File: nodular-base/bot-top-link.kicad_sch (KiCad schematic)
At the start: 9 parts, among them J9 Conn_01x30_MountingPin, U13 MT9700, U6 74LVC1G17

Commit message: WIP layout for base
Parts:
- added C21, C22: 10uF, Capacitor_SMD:C_1206_3216Metric, symbol Device:C
- added D14: SK6805MICRO-J, LED_SMD:LED_SK6805_PLCC4_2.4x2.7mm_P1.3mm, symbol LED:SK6812MINI
- added R22 (x2): 11k3, Resistor_SMD:R_0402_1005Metric, symbol Device:R
- added R22 (x2): 1k, Resistor_SMD:R_0402_1005Metric, symbol Device:R
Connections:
- net GND: now also U13.2 (GND), U6.3 (GND), C21.2, C22.2, D14.2 (VSS), R22.2, R22.2
- net LED_DATA: now reaches U6.2
- net at U6.4: now also R22.1
- net TOP_VBAT_SW: now reaches U6.5 (VCC)
- net TOP_VBAT_SW: now also U13.1 (OUT), C22.1, D14.4 (VDD)
- net at U13.3 (SET): now also R22.1
- net LED_EN: now reaches U13.4 (ON)
- net LED_EN: now also R22.1
- net at U13.5 (IN): now also C21.1
- new net: D14.1 (DOUT), R22.1
- new net: D14.3 (DIN), R22.2
- new net LED_DATA_TOP: R22.2
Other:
- moved on the sheet: U6

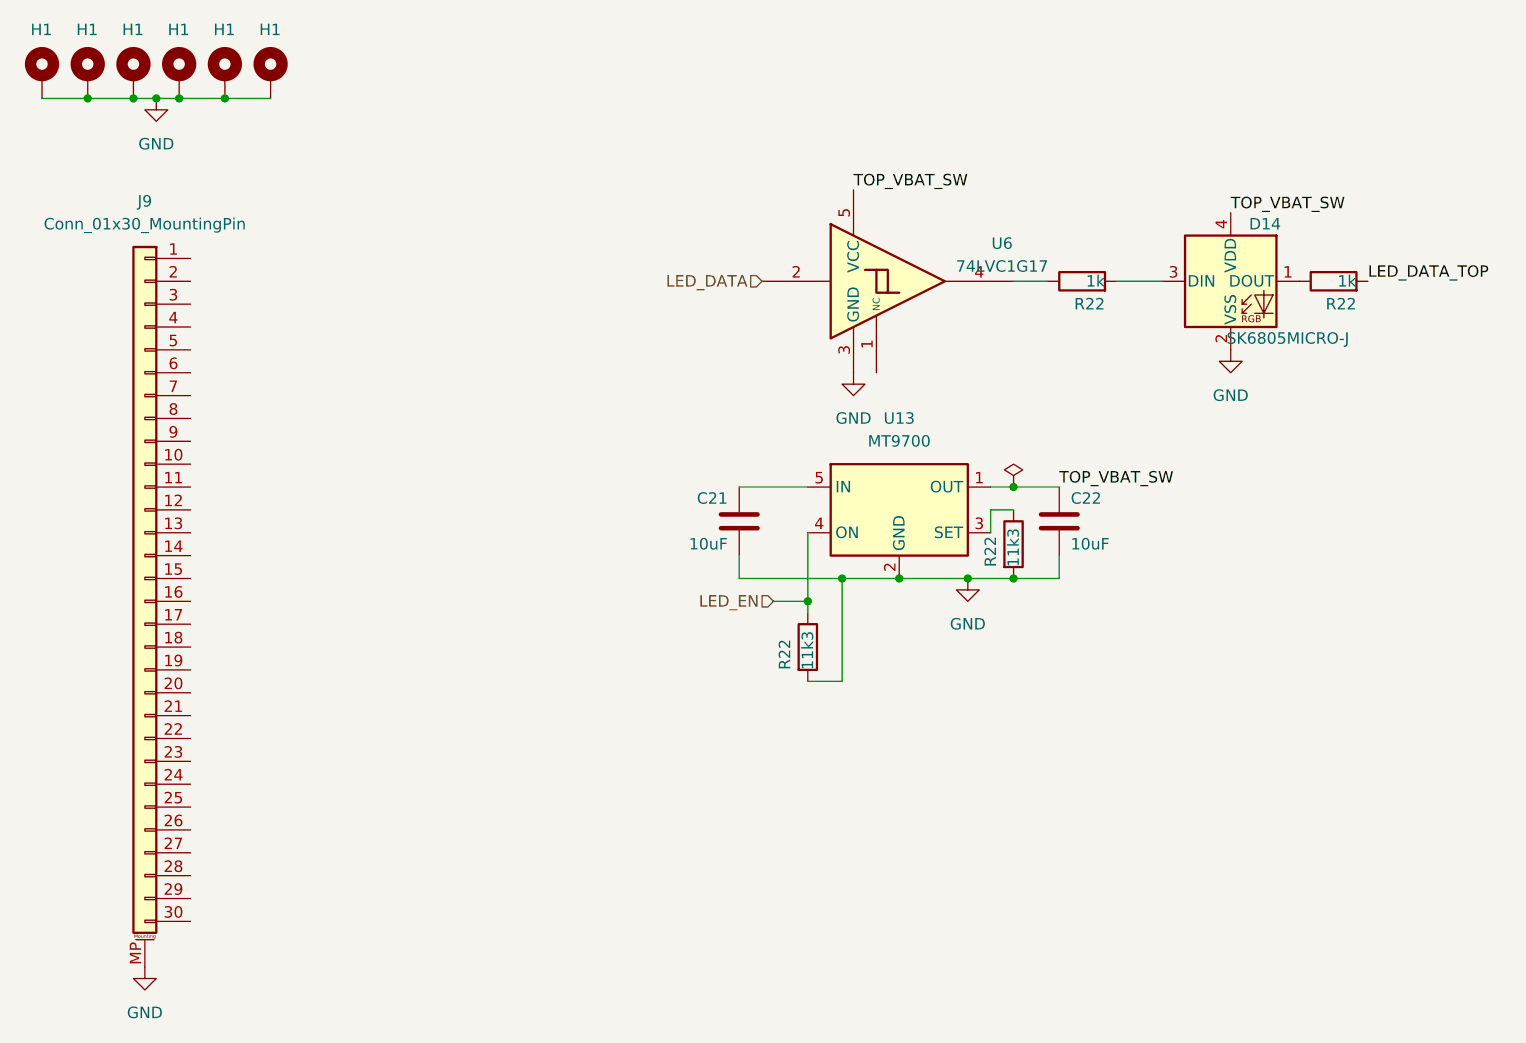
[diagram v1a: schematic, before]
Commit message: Switched from CAN to USB for second USB-C port Added second PD controller and USB mux to allow switching between host and device port Added SOICbite to corner All routing complete Updated pin map, added i2c addresses, soicbit pin mapping, and fpc pinout to document
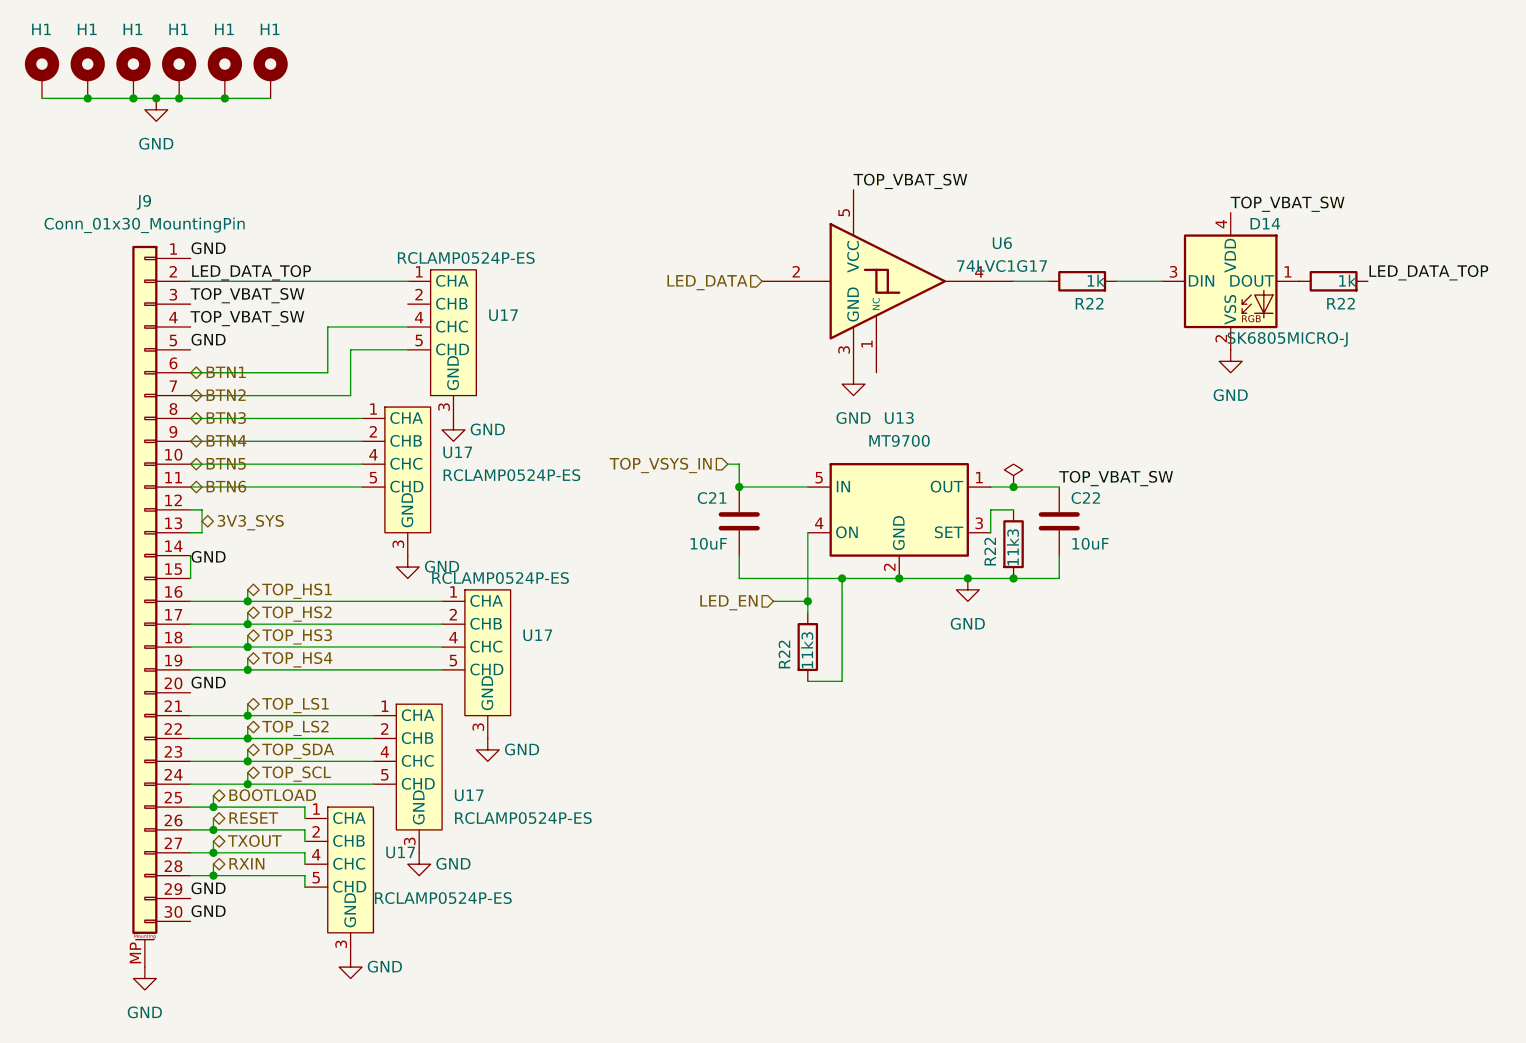
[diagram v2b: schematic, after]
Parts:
- added U17 (x5): RCLAMP0524P-ES, Package_DFN_QFN:Diodes_UDFN-10_1.0x2.5mm_P0.5mm, symbol nodular:RCLAMP0524P-ES
- J9: footprint Connector_FFC-FPC:Hirose_FH12-30S-0.5SH_1x30-1MP_P0.50mm_Horizontal -> nodular:Jushuo_AFC01-S30FCC-00_1x30-1MP_P0.50mm_Horizontal
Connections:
- net GND: now also J9.1 (Pin_1), J9.14 (Pin_14), J9.15 (Pin_15), J9.20 (Pin_20), J9.29 (Pin_29), J9.30 (Pin_30), J9.5 (Pin_5), U17.3 (GND), U17.3 (GND), U17.3 (GND), U17.3 (GND), U17.3 (GND), U17.8 (GND), U17.8 (GND), U17.8 (GND), U17.8 (GND), U17.8 (GND)
- net LED_DATA_TOP: now also J9.2 (Pin_2), U17.1 (CHA), U17.10 (CHA)
- net TOP_VBAT_SW: now also J9.3 (Pin_3), J9.4 (Pin_4)
- net TOP_VSYS_IN: now reaches C21.1, U13.5 (IN)
- net BTN5: now reaches J9.10 (Pin_10)
- net BTN5: now also U17.4 (CHC), U17.7 (CHC)
- net BTN6: now reaches J9.11 (Pin_11)
- net BTN6: now also U17.5 (CHD), U17.6 (CHD)
- net 3V3_SYS: now reaches J9.12 (Pin_12)
- net 3V3_SYS: now also J9.13 (Pin_13)
- net TOP_HS1: now reaches J9.16 (Pin_16)
- net TOP_HS1: now also U17.1 (CHA), U17.10 (CHA)
- net TOP_HS2: now reaches J9.17 (Pin_17)
- net TOP_HS2: now also U17.2 (CHB), U17.9 (CHB)
- net TOP_HS3: now reaches J9.18 (Pin_18)
- net TOP_HS3: now also U17.4 (CHC), U17.7 (CHC)
- net TOP_HS4: now reaches J9.19 (Pin_19)
- net TOP_HS4: now also U17.5 (CHD), U17.6 (CHD)
- net TOP_LS1: now reaches J9.21 (Pin_21)
- net TOP_LS1: now also U17.1 (CHA), U17.10 (CHA)
- net TOP_LS2: now reaches J9.22 (Pin_22)
- net TOP_LS2: now also U17.2 (CHB), U17.9 (CHB)
- net TOP_SDA: now reaches J9.23 (Pin_23)
- net TOP_SDA: now also U17.4 (CHC), U17.7 (CHC)
- net TOP_SCL: now reaches J9.24 (Pin_24)
- net TOP_SCL: now also U17.5 (CHD), U17.6 (CHD)
- net BOOTLOAD: now reaches J9.25 (Pin_25)
- net BOOTLOAD: now also U17.1 (CHA), U17.10 (CHA)
- net RESET: now reaches J9.26 (Pin_26)
- net RESET: now also U17.2 (CHB), U17.9 (CHB)
- net TXOUT: now reaches J9.27 (Pin_27)
- net TXOUT: now also U17.4 (CHC), U17.7 (CHC)
- net RXIN: now reaches J9.28 (Pin_28)
- net RXIN: now also U17.5 (CHD), U17.6 (CHD)
- net BTN1: now reaches J9.6 (Pin_6)
- net BTN1: now also U17.4 (CHC), U17.7 (CHC)
- net BTN2: now reaches J9.7 (Pin_7)
- net BTN2: now also U17.5 (CHD), U17.6 (CHD)
- net BTN3: now reaches J9.8 (Pin_8)
- net BTN3: now also U17.1 (CHA), U17.10 (CHA)
- net BTN4: now reaches J9.9 (Pin_9)
- net BTN4: now also U17.2 (CHB), U17.9 (CHB)
- new net: U17.2 (CHB), U17.9 (CHB)

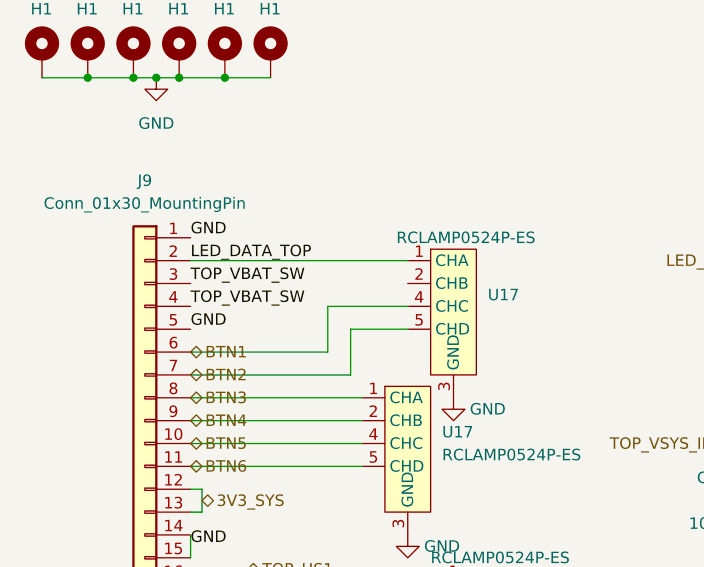
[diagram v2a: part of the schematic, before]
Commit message: Add VCONN support and load switch with 1.5A current limit on host port Add accelerometer interrupt connection Update BOM with important capacitor and inductor PNs and costings
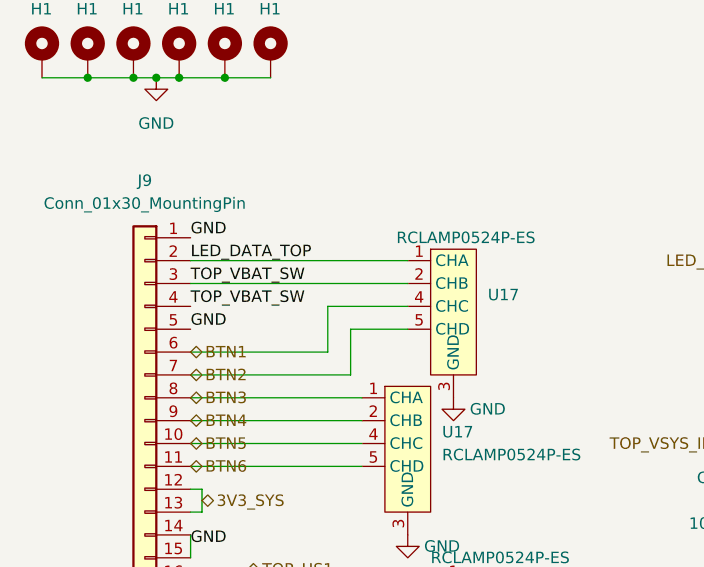
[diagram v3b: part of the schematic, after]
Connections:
- net TOP_VBAT_SW: now also U17.2 (CHB), U17.9 (CHB)
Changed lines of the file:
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@@
+    (stroke (width 0) (type default))
+  )
+  (wire (pts (xy 41.91 52.07) (xy 66.04 52.07))
     (stroke (width 0) (type default))
   )

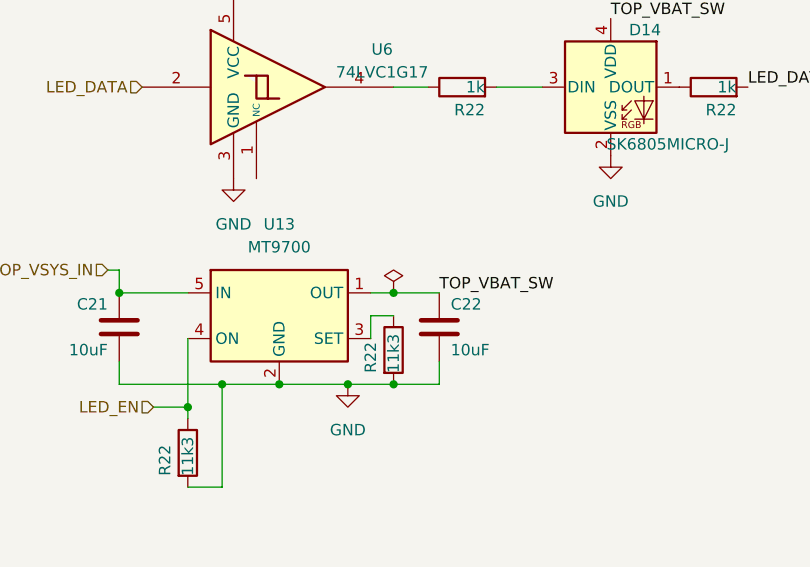
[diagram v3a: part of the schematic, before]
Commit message: Add 3d models and fix erc errors
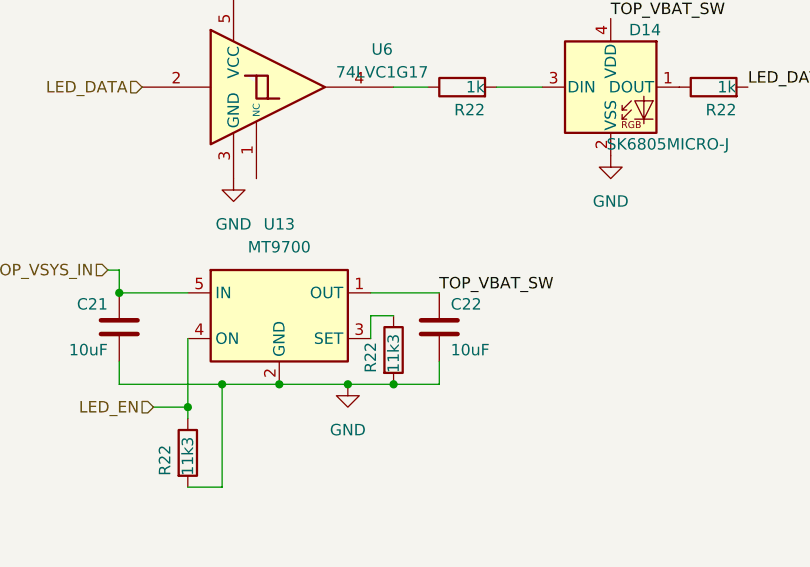
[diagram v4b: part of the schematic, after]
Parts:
- D14: footprint LED_SMD:LED_SK6805_PLCC4_2.4x2.7mm_P1.3mm -> nodular:LED_SK6805_PLCC4_2.4x2.7mm_P1.3mm
- U17: footprint Package_DFN_QFN:Diodes_UDFN-10_1.0x2.5mm_P0.5mm -> nodular:Diodes_UDFN-10_1.0x2.5mm_P0.5mm
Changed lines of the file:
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@@
   (junction (at 110.49 85.09) (diameter 0) (color 0 0 0 0)
   )
-  (junction (at 133.35 72.39) (diameter 0) (color 0 0 0 0)
-  )
   (junction (at 48.26 97.79) (diameter 0) (color 0 0 0 0)
   )
@@
     (stroke (width 0) (type default))
   )
-  (wire (pts (xy 130.81 72.39) (xy 133.35 72.39))
+  (wire (pts (xy 130.81 72.39) (xy 138.43 72.39))
     (stroke (width 0) (type default))
   )
@@
   )
   (wire (pts (xy 44.45 114.3) (xy 44.45 115.57))
-    (stroke (width 0) (type default))
-  )
-  (wire (pts (xy 133.35 72.39) (xy 138.43 72.39))
     (stroke (width 0) (type default))
   )
@@
       (effects (font (size 1.27 1.27)))
     )
-    (property "Footprint" "LED_SMD:LED_SK6805_PLCC4_2.4x2.7mm_P1.3mm" (at 158.75 57.15 0)
+    (property "Footprint" "nodular:LED_SK6805_PLCC4_2.4x2.7mm_P1.3mm" (at 158.75 57.15 0)
       (effects (font (size 1.27 1.27)) (justify left top) hide)
     )
@@
     )
   )
-  (symbol (lib_id "power:PWR_FLAG") (at 133.35 72.39 0) (unit 1)
-    (in_bom yes) (on_board yes) (dnp no) (fields_autoplaced)
-    (property "Reference" "#FLG06" (at 133.35 70.485 0)
-      (effects (font (size 1.27 1.27)) hide)
-    )
-    (property "Value" "PWR_FLAG" (at 133.35 67.31 0)
-      (effects (font (size 1.27 1.27)) hide)
-    )
-    (property "Footprint" "" (at 133.35 72.39 0)
-      (effects (font (size 1.27 1.27)) hide)
-    )
-    (property "Datasheet" "~" (at 133.35 72.39 0)
-      (effects (font (size 1.27 1.27)) hide)
-    )
-    (pin "1")
-    (instances
-      (project "nodular-base"
-        (path "/6dcb0502-87e2-4c28-9ce8-81aab8925f06/6fb70d96-9605-4ce0-8240-c18acdf3484a"
-          (reference "#FLG06") (unit 1)
-        )
-        (path "/6dcb0502-87e2-4c28-9ce8-81aab8925f06/35334d26-c60a-4490-bcdf-fce7d9c2e66d"
-          (reference "#FLG07") (unit 1)
-        )
-      )
-    )
-  )
   (symbol (lib_id "power:GND") (at 59.69 124.46 0) (unit 1)
     (in_bom yes) (on_board yes) (dnp no)
@@
       (effects (font (size 1.27 1.27)) (justify left))
     )
-    (property "Footprint" "Package_DFN_QFN:Diodes_UDFN-10_1.0x2.5mm_P0.5mm" (at 71.12 54.61 0)
+    (property "Footprint" "nodular:Diodes_UDFN-10_1.0x2.5mm_P0.5mm" (at 71.12 54.61 0)
       (effects (font (size 1.27 1.27)) hide)
     )
@@
       (effects (font (size 1.27 1.27)) (justify left))
     )
-    (property "Footprint" "Package_DFN_QFN:Diodes_UDFN-10_1.0x2.5mm_P0.5mm" (at 67.31 102.87 0)
+    (property "Footprint" "nodular:Diodes_UDFN-10_1.0x2.5mm_P0.5mm" (at 67.31 102.87 0)
       (effects (font (size 1.27 1.27)) hide)
     )
@@
       (effects (font (size 1.27 1.27)) (justify left))
     )
-    (property "Footprint" "Package_DFN_QFN:Diodes_UDFN-10_1.0x2.5mm_P0.5mm" (at 74.93 90.17 0)
+    (property "Footprint" "nodular:Diodes_UDFN-10_1.0x2.5mm_P0.5mm" (at 74.93 90.17 0)
       (effects (font (size 1.27 1.27)) hide)
     )
@@
       (effects (font (size 1.27 1.27)) (justify left))
     )
-    (property "Footprint" "Package_DFN_QFN:Diodes_UDFN-10_1.0x2.5mm_P0.5mm" (at 66.04 69.85 0)
+    (property "Footprint" "nodular:Diodes_UDFN-10_1.0x2.5mm_P0.5mm" (at 66.04 69.85 0)
       (effects (font (size 1.27 1.27)) hide)
     )
@@
       (effects (font (size 1.27 1.27)) (justify left))
     )
-    (property "Footprint" "Package_DFN_QFN:Diodes_UDFN-10_1.0x2.5mm_P0.5mm" (at 59.69 114.3 0)
-      (effects (font (size 1.27 1.27)) hide)
-    )
+    (property "Footprint" "nodular:Diodes_UDFN-10_1.0x2.5mm_P0.5mm" (at 59.69 114.3 0)
+      (effects (font (size 1.27 1.27)) hide)
+    )
